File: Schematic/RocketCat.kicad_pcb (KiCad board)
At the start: 2 copper layers, 1 part, among them U1 WeMos_mini

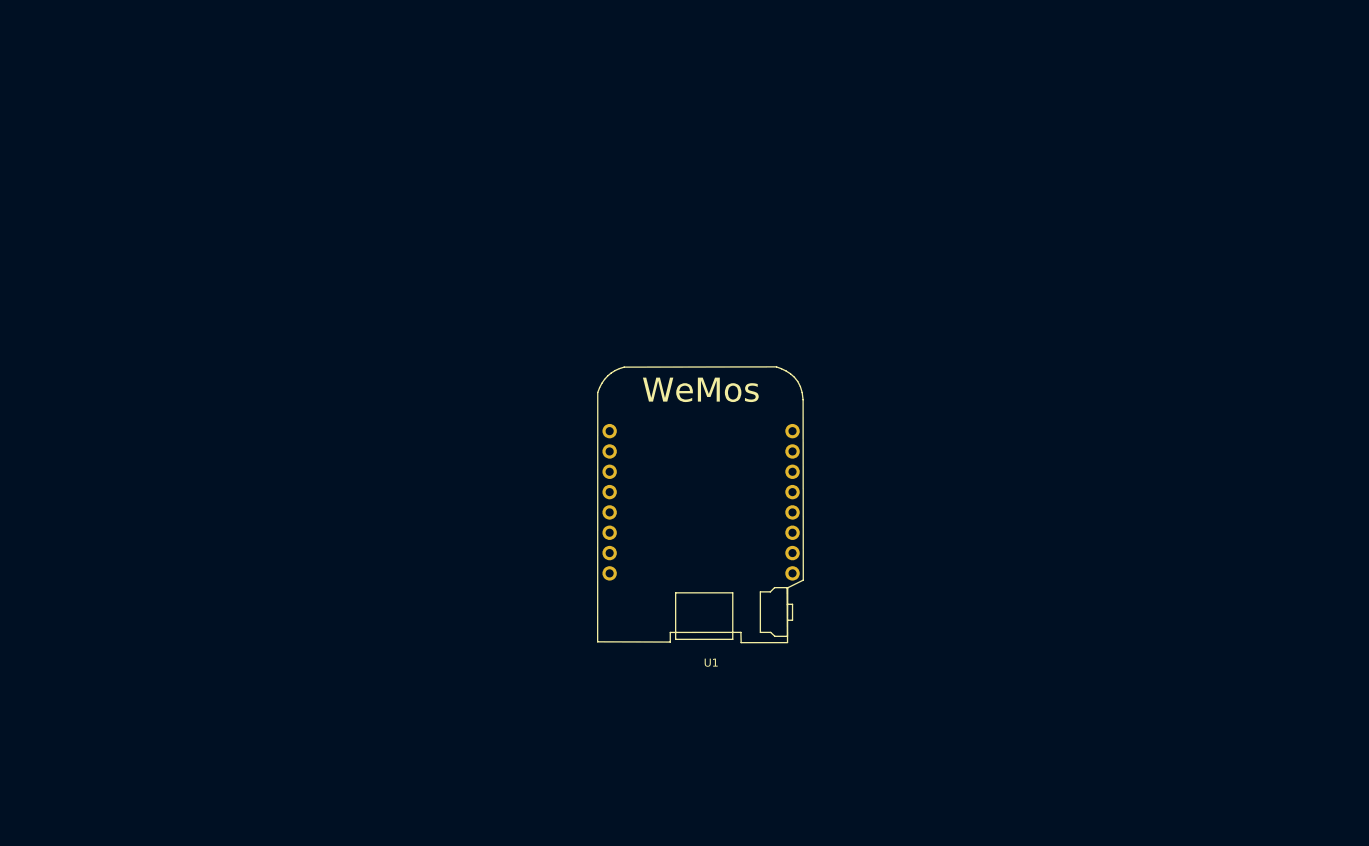
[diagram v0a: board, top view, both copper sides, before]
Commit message: Agregado Bateria y gy 87
en lo de la pbc me falta un pista, lo podrias poner pof favor xd
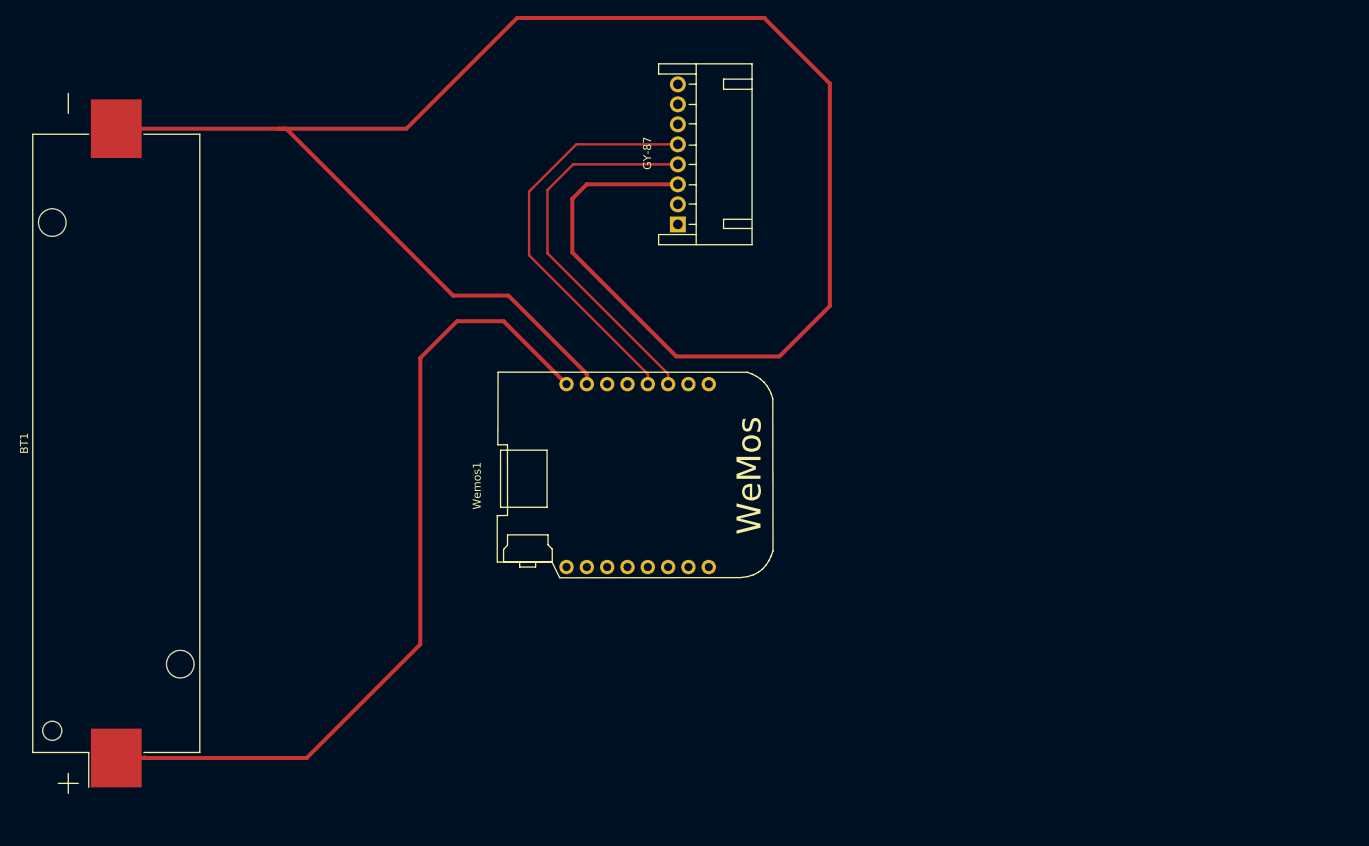
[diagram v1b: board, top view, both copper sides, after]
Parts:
- removed U1: WeMos_mini, wemos_d1_mini:D1_mini_board
- added BT1: Bateria, Battery_Holders:Keystone_1042_1x18650, F.Cu at (75.4, 96.4)
- added GY-87: Conn_01x08, Connectors:Wafer_Horizontal22.5x5.8x7RM2.5-8, F.Cu at (145.6, 69.0)
- added Wemos1: WeMos_mini, wemos_d1_mini:D1_mini_board, F.Cu at (139.3, 100.4)
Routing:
- net Net-(BT1-Pad2): track 0.00 -> 242.5 mm
- net Net-(BT1-Pad1): track 0.00 -> 106.7 mm
- net Net-(GY-87-Pad5): track 0.00 -> 51.3 mm
- net Net-(GY-87-Pad4): track 0.00 -> 48.1 mm
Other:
- net class ElectroniCats Pista added: clearance 0.2, trace_width 0.3, via_dia 0.6, via_drill 0.4
- net class ElectroniCats VCC added: clearance 0.2, trace_width 0.5, via_dia 0.6, via_drill 0.4

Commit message: PCB Lista
Checar si no tengo nada mal
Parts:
- removed BT1: Bateria, Battery_Holders:Keystone_1042_1x18650
- added D1: LED, LEDs:LED_0805, F.Cu at (140.4, 119.4)
- added D2: D_Schottky, Diodes_SMD:D_0805, F.Cu at (155.9, 115.9)
- added D3: D, Diodes_SMD:D_0805, F.Cu at (149.9, 136.1)
- added J1: Conn_01x08, Socket_Strips:Socket_Strip_Straight_1x08_Pitch2.54mm, F.Cu at (194.5, 141.4)
- added J2: Conn_01x02, Socket_Strips:Socket_Strip_Straight_1x02_Pitch2.54mm, F.Cu at (160.0, 142.0)
- added R1: 1k, Resistors_SMD:R_0805, F.Cu at (155.4, 126.5)
- added R2: 10K, Resistors_SMD:R_0805, F.Cu at (150.1, 120.5)
- added U1: MCP73831T-4ADI/OT, TO_SOT_Packages_SMD:SOT-23-5, F.Cu at (145.4, 129.2)
- GY-87: footprint Connectors:Wafer_Horizontal22.5x5.8x7RM2.5-8 -> Socket_Strips:Socket_Strip_Straight_1x08_Pitch2.54mm
- moved GY-87 50.2 mm to (195.5, 75.2), turned to 270 degrees
- moved Wemos1 47.3 mm to (186.3, 105.7), turned to 0 degrees
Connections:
- net Net-(BT1-Pad2) renamed GND
- net Net-(GY-87-Pad2) renamed +3V3
- net Net-(GY-87-Pad4) renamed /D1
- net Net-(GY-87-Pad5) renamed /D2
- Wemos1 pad 1: Net-(BT1-Pad1) -> VCC
- Wemos1 pad 10: Net-(Wemos1-Pad10) -> /A0
- Wemos1 pad 11: Net-(Wemos1-Pad11) -> /D0
- Wemos1 pad 12: Net-(Wemos1-Pad12) -> /D5
- Wemos1 pad 13: Net-(Wemos1-Pad13) -> /D6
- Wemos1 pad 14: Net-(Wemos1-Pad14) -> /D7
- Wemos1 pad 15: Net-(Wemos1-Pad15) -> /D8
- Wemos1 pad 3: Net-(Wemos1-Pad3) -> /D4
- Wemos1 pad 4: Net-(Wemos1-Pad4) -> /D3
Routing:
- net Net-(BT1-Pad1): track 106.7 -> 0.00 mm
- net GND: track 242.5 -> 172.6 mm
- net VCC: track 0.00 -> 63.1 mm
- net +BATT: track 0.00 -> 52.9 mm
- net /A0: track 0.00 -> 51.6 mm
- net /D0: track 0.00 -> 50.9 mm
- net /D5: track 0.00 -> 44.9 mm
- net /D6: track 0.00 -> 41.7 mm
- net /D7: track 0.00 -> 41.4 mm
- net Net-(R2-Pad2): track 0.00 -> 40.9 mm
- net +3V3: track 0.00 -> 40.1 mm
- net /D8: track 0.00 -> 38.6 mm
- net /D3: track 0.00 -> 36.5 mm
- net /D4: track 0.00 -> 35.0 mm
- net /D1: track 48.1 -> 33.7 mm
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
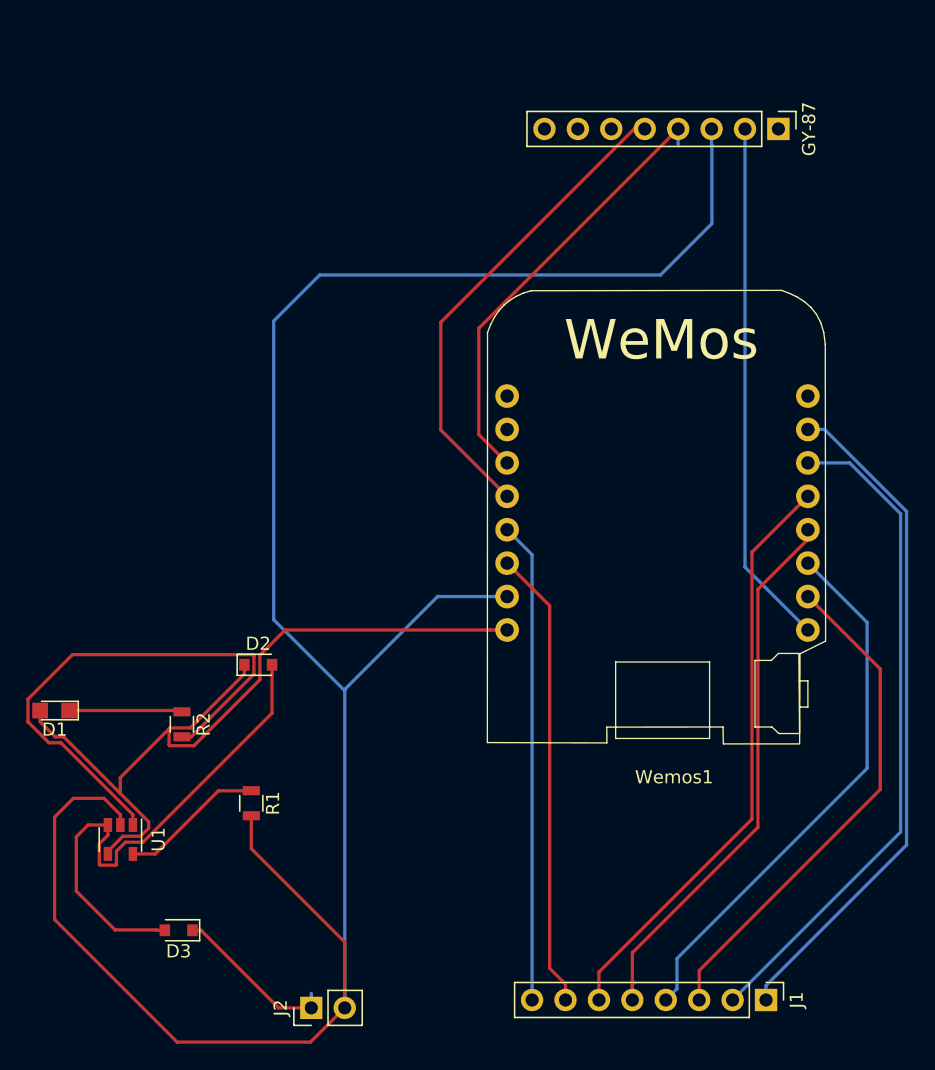
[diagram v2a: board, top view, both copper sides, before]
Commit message: Pcb aun no lista. v.0.1
Se redujo el espacio, para no desperdiciarlo.
Arreglo de pistas de 0.25mm a 0.3mm
Espacio definido para el GY87
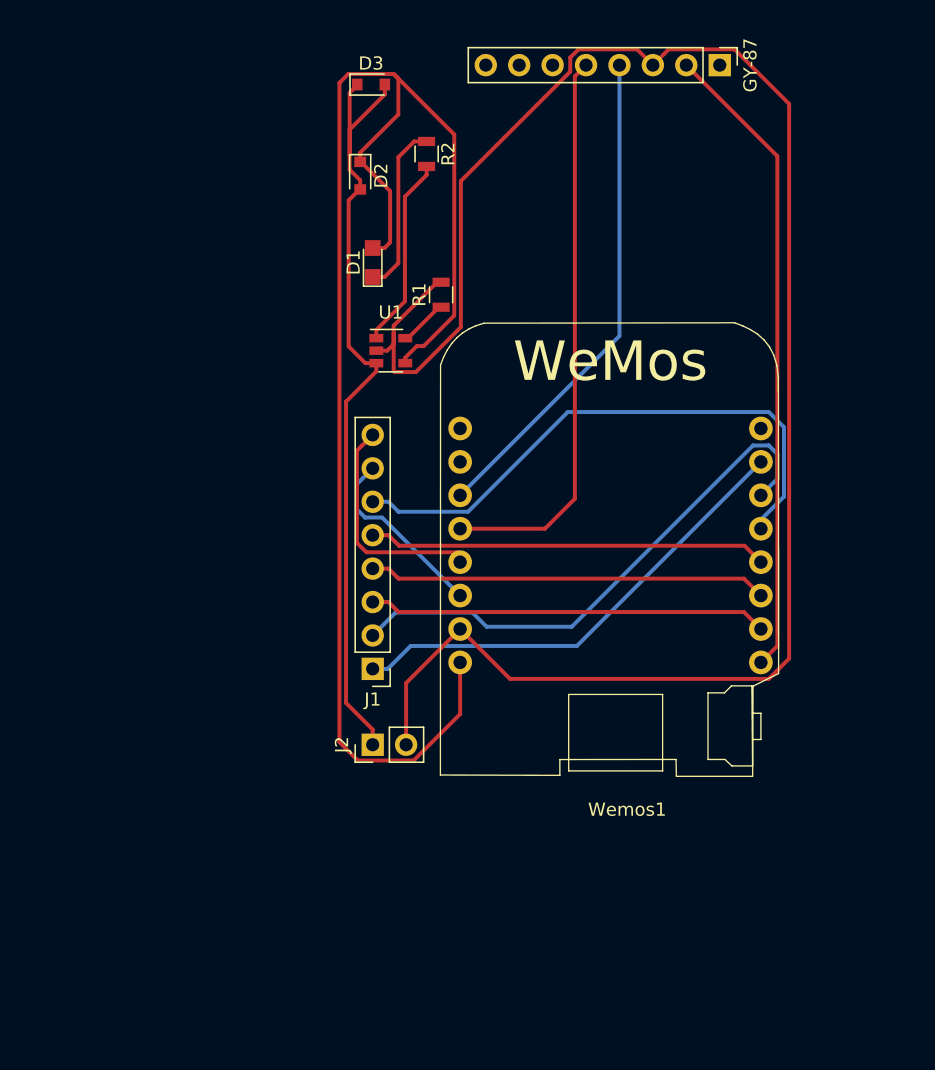
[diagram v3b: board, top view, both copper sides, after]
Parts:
- moved D3 65.9 mm to (164.5, 71.8), turned to 0 degrees
- moved R2 47.2 mm to (168.7, 77.1)
- moved U1 42.5 mm to (166.0, 92.0), turned to 0 degrees
- moved D1 41.8 mm to (164.6, 85.3), turned to 90 degrees
- moved R1 41.3 mm to (169.8, 87.8), turned to 90 degrees
- moved J1 39.1 mm to (164.6, 116.2), turned to 180 degrees
- moved D2 38.0 mm to (163.7, 78.8), turned to 270 degrees
- moved J2 20.5 mm to (164.6, 122.0)
- moved GY-87 6.59 mm to (191.0, 70.3)
- moved Wemos1 4.34 mm to (182.7, 108.1)
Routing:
- net VCC: track 63.1 -> 112.0 mm
- net GND: track 172.6 -> 140.7 mm
- net Net-(R2-Pad2): track 40.9 -> 14.6 mm
- net /D4: track 35.0 -> 14.2 mm
- net /D3: track 36.5 -> 17.5 mm
- net /A0: track 51.6 -> 36.0 mm
- net /D6: track 41.7 -> 30.4 mm
- net /D7: track 41.4 -> 30.4 mm
- net /D0: track 50.9 -> 41.6 mm
- net +3V3: track 40.1 -> 48.8 mm
- net /D8: track 38.6 -> 30.4 mm
- net +BATT: track 52.9 -> 60.7 mm
- net Net-(R1-Pad1): track 11.0 -> 3.70 mm
- net /D2: track 36.9 -> 43.0 mm
- net Net-(D1-Pad1): track 8.62 -> 13.1 mm
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
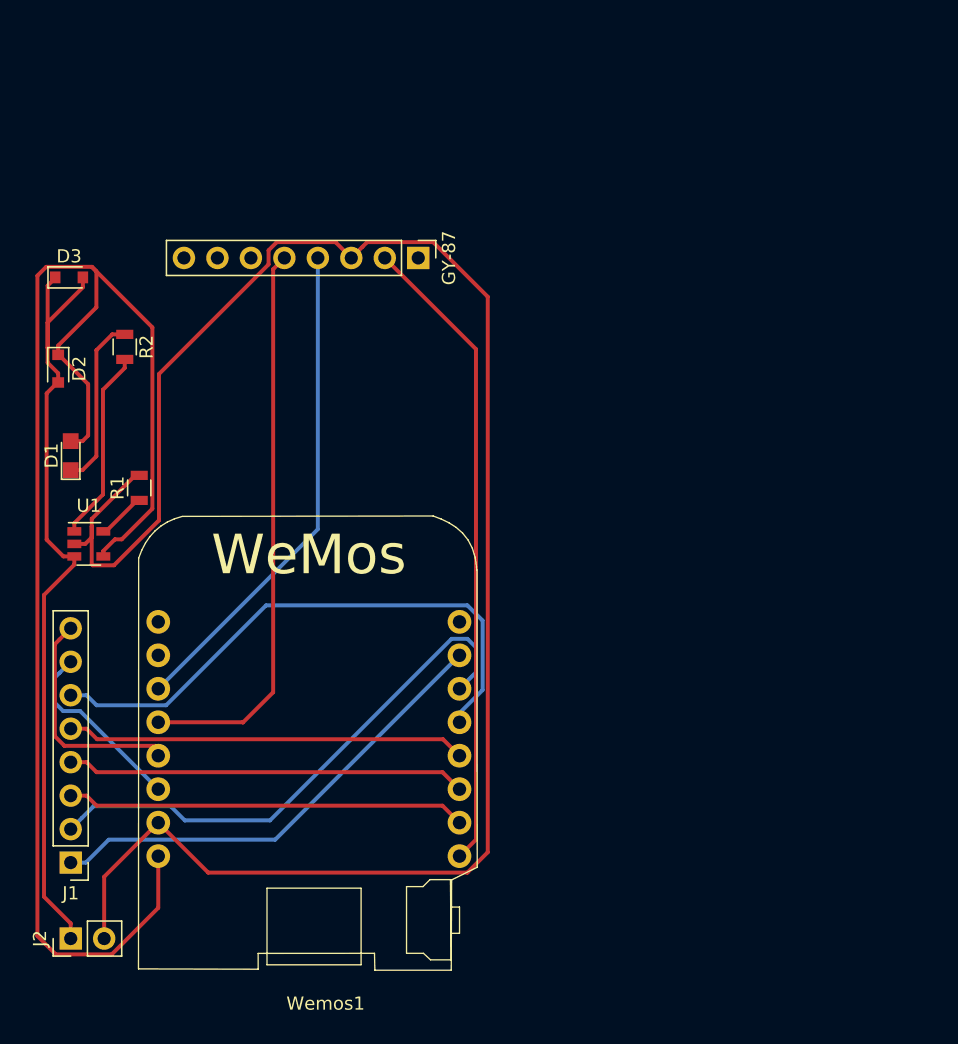
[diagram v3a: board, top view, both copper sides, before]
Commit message: fix size and tracks remove MCP charger
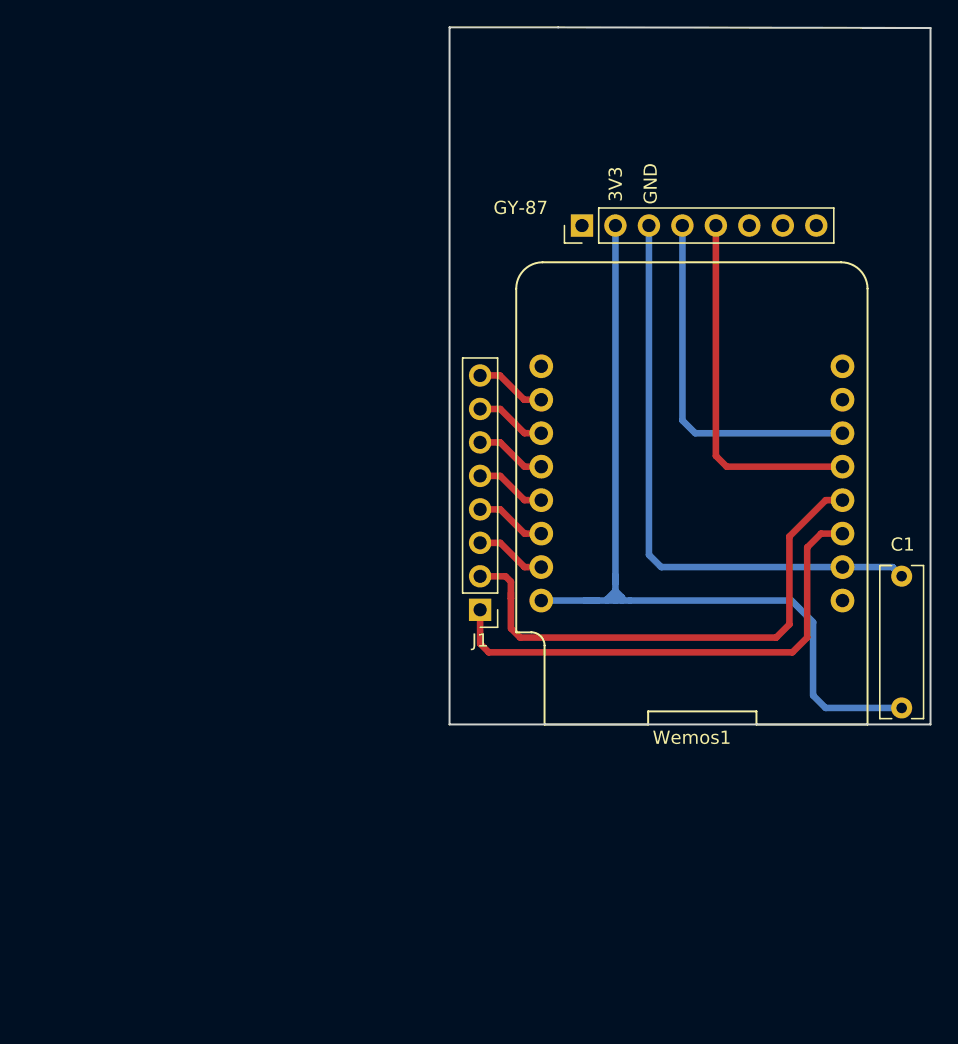
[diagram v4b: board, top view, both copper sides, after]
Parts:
- removed D1: LED, LEDs:LED_0805
- removed D2: D_Schottky, Diodes_SMD:D_0805
- removed D3: D, Diodes_SMD:D_0805
- removed J2: Conn_01x02, Socket_Strips:Socket_Strip_Straight_1x02_Pitch2.54mm
- removed R1: 1k, Resistors_SMD:R_0805
- removed R2: 10K, Resistors_SMD:R_0805
- removed U1: MCP73831T-4ADI/OT, TO_SOT_Packages_SMD:SOT-23-5
- added C1: 0.1uF, Capacitors_THT:C_Rect_L11.5mm_W3.2mm_P10.00mm_MKT, F.Cu at (227.7, 104.5)
- Wemos1: footprint wemos_d1_mini:D1_mini_board -> wemos-d1-mini:wemos-d1-mini-connectors-only
- moved J1 36.5 mm to (195.7, 97.0)
- moved Wemos1 35.7 mm to (211.8, 87.5), turned to 90 degrees
- moved GY-87 12.7 mm to (203.4, 67.9), turned to 90 degrees
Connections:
- J1 pad 1: /A0 -> /D4
- J1 pad 2: /D0 -> /D3
- J1 pad 7: /D4 -> /D0
- J1 pad 8: /D3 -> /A0
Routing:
- net VCC: track 112.0 -> 0.00 mm
- net GND: track 140.7 -> 44.8 mm
- net +BATT: track 60.7 -> 0.00 mm
- net /D5: track 44.6 -> 5.40 mm
- net /D0: track 41.6 -> 5.40 mm
- net /A0: track 36.0 -> 5.40 mm
- net /D7: track 30.4 -> 5.40 mm
- net /D8: track 30.4 -> 5.40 mm
- net /D6: track 30.4 -> 5.40 mm
- net /D4: track 14.2 -> 38.1 mm
- net /D3: track 17.5 -> 40.2 mm
- net +3V3: track 48.8 -> 65.9 mm
- net /D2: track 43.0 -> 27.4 mm
- net Net-(R2-Pad2): track 14.6 -> 0.00 mm
- net Net-(D1-Pad1): track 13.1 -> 0.00 mm
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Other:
- board outline added: 36.5 x 52.9 mm
- net class Default: trace_width 0.25 -> 0.5
- board text added: "3V3"
- board text added: "GND"

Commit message: Añadido logo de EC
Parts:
- added G***: LOGO, TIH:electronic_cats_logo_8x6, F.Cu at (197.9, 59.8)
